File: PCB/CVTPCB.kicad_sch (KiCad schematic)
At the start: 13 parts, among them J1 Conn_01x09_Pin, J4 2x1, J7 SystemInput

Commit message: Add files via upload
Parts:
- removed C1: 0.1uf, symbol Device:C
- removed J1: Conn_01x09_Pin, symbol Connector:Conn_01x09_Pin
- removed R3, R4: R, symbol Device:R
- removed R5, R6: 22, symbol Device:R
- removed R7: 100k, symbol Device:R
- added C2, C3: 0.1uf, Capacitor_THT:C_Disc_D3.0mm_W2.0mm_P2.50mm, symbol Device:C
- added H1, H2, H3, H4: MountingHole, MountingHole:MountingHole_4.3mm_M4, symbol Mechanical:MountingHole
- added J1, J3: Infared, CVT:Infared, symbol Connector:Conn_01x04_Pin
- added J2, J5: TMP36, CVT:TMP36_Pad, symbol Connector:Conn_01x03_Pin
- added R10, R8: 300, Resistor_THT:R_Axial_DIN0204_L3.6mm_D1.6mm_P5.08mm_Horizontal, symbol Device:R
- added R11, R9: 200, Resistor_THT:R_Axial_DIN0204_L3.6mm_D1.6mm_P5.08mm_Horizontal, symbol Device:R
- added R12: 22, Resistor_THT:R_Axial_DIN0204_L3.6mm_D1.6mm_P5.08mm_Horizontal, symbol Device:R
- added R13: R, Resistor_THT:R_Axial_DIN0204_L3.6mm_D1.6mm_P5.08mm_Horizontal, symbol Device:R
- added RV1, RV2: 0-10k, Potentiometer_THT:Potentiometer_Bourns_3339H_Vertical, symbol Device:R_Potentiometer
- J4: footprint CONN_S2B-PH-K-S_JST -> Connector_PinHeader_1.00mm:PinHeader_1x02_P1.00mm_Vertical
- J7: footprint (none) -> CVT:JST4Pin
- R1: value 200 -> R; footprint (none) -> Resistor_THT:R_Axial_DIN0204_L3.6mm_D1.6mm_P5.08mm_Horizontal
- R2: value 300 -> 22; footprint (none) -> Resistor_THT:R_Axial_DIN0204_L3.6mm_D1.6mm_P5.08mm_Horizontal
- U3: footprint ESP 32:ESP 32 BAJA -> CVT:ESP 32 BAJA
- U4: footprint (none) -> CVT:1x7 Connectors
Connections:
- net +5V: now also R2.2, J1.1 (IR+), J2.2 (3.3+), J3.1 (IR+), J5.2 (3.3+), R12.2
- net CanRX: now also U3.24 (D26); no longer U3.14 (D22)
- net CanTX: now also U3.25 (D27); no longer U3.11 (D21)
- net GND: now also C2.1, C3.1, J1.3 (E-), J2.3 (GND), J3.3 (E-), J5.3 (GND), R10.2, R8.2, RV1.3, RV2.3; no longer R2.2
- net at R1.1: now also J1.2 (IR-)
- net TMP36_2: now reaches U3.27 (D12)
- net TMP36_2: now also R8.1, R9.2
- net TMP36_1: now reaches U3.28 (D13)
- net TMP36_1: now also R10.1, R11.2
- net E-1 renamed Ir1
- net Ir1: now also R13.2, RV1.1, RV1.2
- net E-2 renamed Ir2
- net Ir2: now also R1.2, RV2.1, RV2.2
- net R+1: no longer names the net of U3.22 (D33)
- net R+2: no longer names the net of U3.21 (D32)
- removed net TMP36_out: R1.2, R2.1, U3.25 (D27)
- new net: J3.2 (IR-), R13.1
- new net: J3.4 (E+), R12.1
- new net: J1.4 (E+), R2.1
- new net: C3.2, J5.1 (s), R11.1
- new net: C2.2, J2.1 (s), R9.1
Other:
- moved on the sheet: J4, J7, U3, U4

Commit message: Add files via upload
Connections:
- net CanTX: now also U3.23 (D25); no longer U3.25 (D27)
- net Ir2: now also U3.28 (D13); no longer U3.19 (D34)
- net TMP36_1: now also U3.19 (D34); no longer U3.28 (D13)
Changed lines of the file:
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@@
+	(wire
+		(pts
+			(xy 113.03 73.66) (xy 115.57 73.66)
+		)
+		(stroke
+			(width 0)
+			(type default)
+		)
+	)
 	(wire
 		(pts
@@
 	(wire
 		(pts
-			(xy 113.03 99.06) (xy 115.57 99.06)
-		)
-		(stroke
-			(width 0)
-			(type default)
-		)
-	)
-	(wire
-		(pts
 			(xy 156.21 148.59) (xy 167.64 148.59)
 		)
@@
 	(wire
 		(pts
-			(xy 113.03 73.66) (xy 115.57 73.66)
-		)
-		(stroke
-			(width 0)
-			(type default)
-		)
-	)
-	(wire
-		(pts
 			(xy 140.97 63.5) (xy 140.97 64.77)
 		)
@@
 	(wire
 		(pts
+			(xy 113.03 93.98) (xy 115.57 93.98)
+		)
+		(stroke
+			(width 0)
+			(type default)
+		)
+	)
+	(wire
+		(pts
 			(xy 148.59 135.89) (xy 151.13 135.89)
 		)
@@
 		)
 	)
-	(label "TMP36_1"
+	(label "Ir2"
 		(at 115.57 73.66 0)
+		(fields_autoplaced yes)
+		(effects
+			(font
+				(size 1.27 1.27)
+			)
+			(justify left bottom)
+		)
+	)
+	(label "CanTX"
+		(at 115.57 93.98 0)
 		(fields_autoplaced yes)
 		(effects
@@
 		)
 	)
-	(label "CanTX"
-		(at 115.57 99.06 0)
-		(fields_autoplaced yes)
-		(effects
-			(font
-				(size 1.27 1.27)
-			)
-			(justify left bottom)
-		)
-	)
 	(label "CanL"
 		(at 140.97 87.63 180)
@@
 		)
 	)
-	(label "Ir2"
-		(at 115.57 106.68 0)
-		(fields_autoplaced yes)
-		(effects
-			(font
-				(size 1.27 1.27)
-			)
-			(justify left bottom)
-		)
-	)
 	(label "CanTX"
 		(at 137.16 76.2 180)
@@
 		(fields_autoplaced yes)
 		(effects
+			(font
+				(size 1.27 1.27)
+			)
+			(justify left bottom)
+		)
+	)
+	(label "TMP36_1"
+		(at 115.57 106.68 0)
+		(fields_autoplaced yes)
+		(effects

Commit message: Add files via upload
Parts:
- removed J4: 2x1, Connector_PinHeader_1.00mm:PinHeader_1x02_P1.00mm_Vertical, symbol 2x1:S2B-PH-K-SLFSN
- removed R13: R, Resistor_THT:R_Axial_DIN0204_L3.6mm_D1.6mm_P5.08mm_Horizontal, symbol Device:R
- added J4: Conn_01x04_Pin, CVT:PowerBoard, symbol Connector:Conn_01x04_Pin
- added R3: R, Resistor_THT:R_Axial_DIN0411_L9.9mm_D3.6mm_P12.70mm_Horizontal, symbol Device:R
- R1, R10, R11, R12, R2, R8, R9: footprint Resistor_THT:R_Axial_DIN0204_L3.6mm_D1.6mm_P5.08mm_Horizontal -> Resistor_THT:R_Axial_DIN0411_L9.9mm_D3.6mm_P12.70mm_Horizontal
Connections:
- net +5V: now also J4.1 (Pin_1); no longer J1.1 (IR+)
- net GND: now also R1.2, RV1.1, RV2.1, J4.2 (Pin_2), J4.4 (Pin_4), R3.2; no longer J1.3 (E-), RV1.3, RV2.3
- net Ir1: no longer RV1.1
- net Ir2: no longer R1.2, RV2.1
- net IrOut2: now reaches J3.2 (IR-)
- net IrOut2: now also RV1.3, U3.26 (D14), R3.1
- net IrOut1: now reaches J1.2 (IR-), R1.1
- net IrOut1: now also RV2.3, U3.22 (D33)
- net +12V renamed +12v
- net +12v: now also J4.3 (Pin_3)

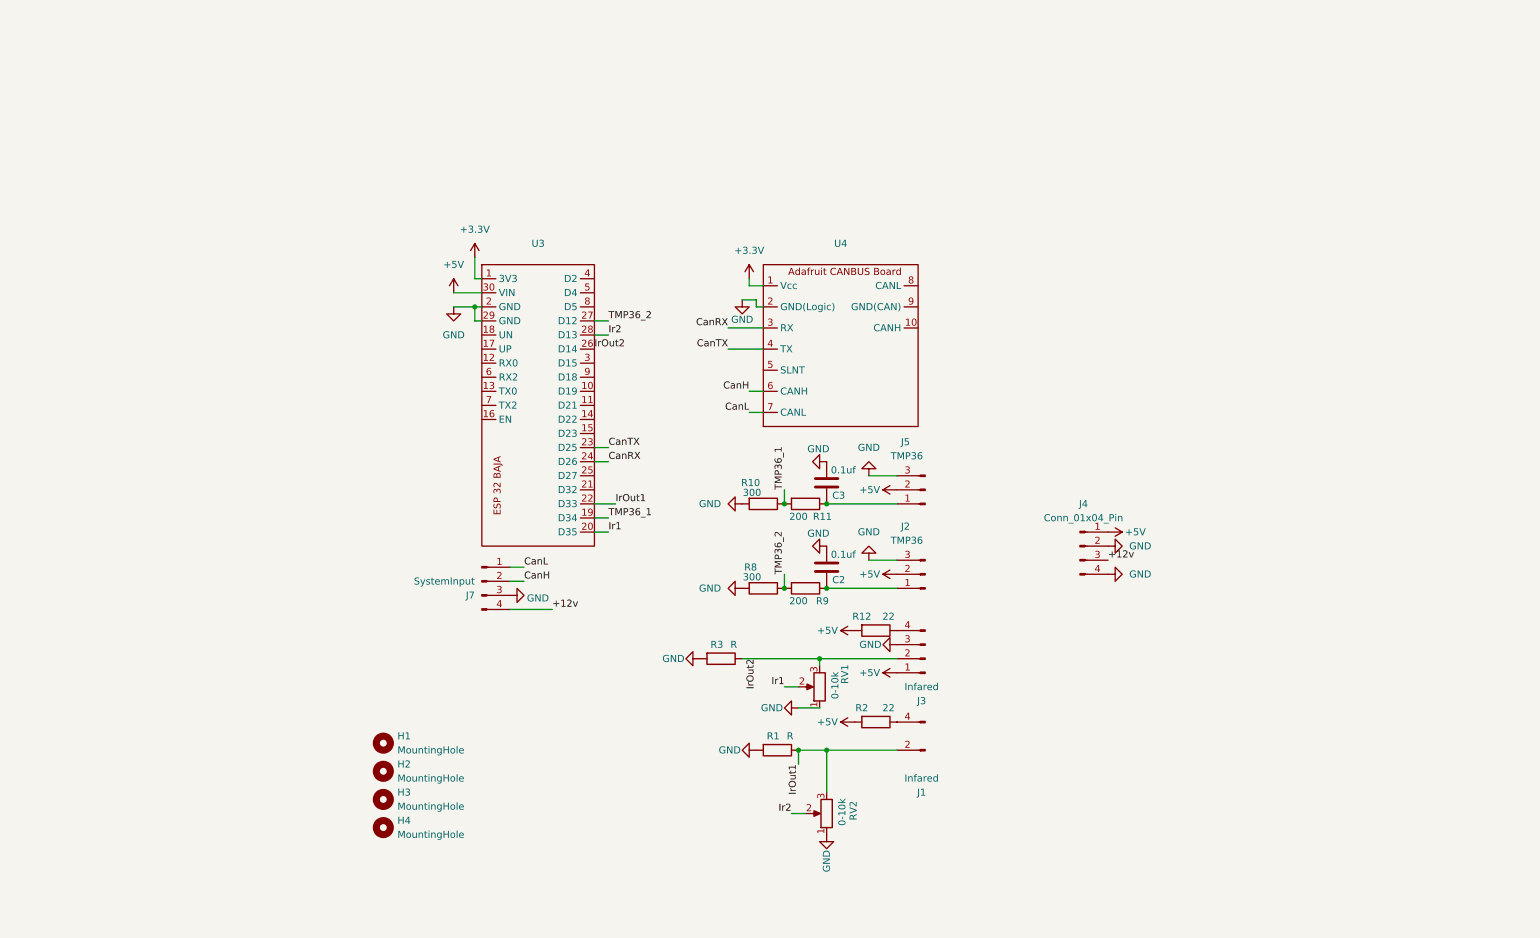
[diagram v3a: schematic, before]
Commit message: Various changes to PCB design
Changes:
Move 4 pin aviation plug connector to bottom of PCB
Move 0.1uF bypass capacitors from Vout to Vs
Remove voltage divider on TMP36 output. TMP36 output ranges from 0.1V to 2.0V, which is within our 0-3.3V reading range on ESP32
Change signal voltage divider for IR receiver from 1W footprint to 1/4W footprint
Combine +5V and GND pads for IR and TMP36
Update Silkscreen and Labels for clarity
Make Power pads SMD
Move all components to top side
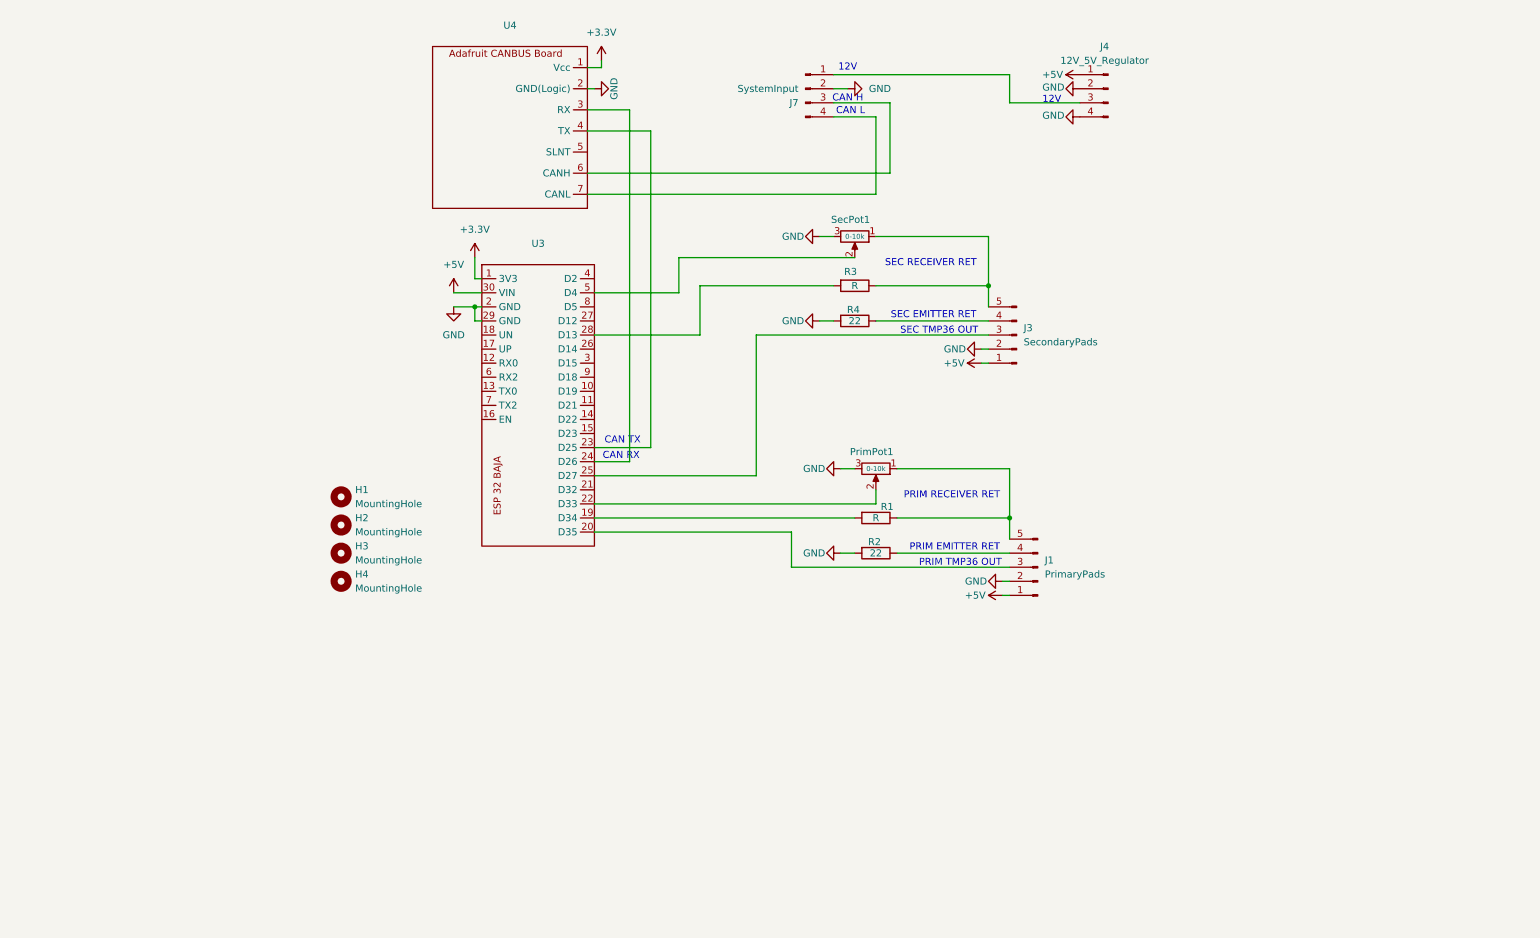
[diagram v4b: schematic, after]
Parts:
- removed C2, C3: 0.1uf, Capacitor_THT:C_Disc_D3.0mm_W2.0mm_P2.50mm, symbol Device:C
- removed J1: Infared, CVT:Infared, symbol Connector:Conn_01x04_Pin
- removed J2, J5: TMP36, CVT:TMP36_Pad, symbol Connector:Conn_01x03_Pin
- removed R10, R8: 300, Resistor_THT:R_Axial_DIN0411_L9.9mm_D3.6mm_P12.70mm_Horizontal, symbol Device:R
- removed R11, R9: 200, Resistor_THT:R_Axial_DIN0411_L9.9mm_D3.6mm_P12.70mm_Horizontal, symbol Device:R
- removed R12: 22, Resistor_THT:R_Axial_DIN0411_L9.9mm_D3.6mm_P12.70mm_Horizontal, symbol Device:R
- removed RV2: 0-10k, Potentiometer_THT:Potentiometer_Bourns_3339H_Vertical, symbol Device:R_Potentiometer
- added J1: PrimaryPads, CVT:Temp_IR_5_Pad_Combo, symbol Connector:Conn_01x05_Pin
- added PrimPot1: 0-10k, Potentiometer_THT:Potentiometer_Bourns_3339H_Vertical, symbol Device:R_Potentiometer
- added R4: 22, Resistor_THT:R_Axial_DIN0411_L9.9mm_D3.6mm_P12.70mm_Horizontal, symbol Device:R
- J3: value Infared -> SecondaryPads; footprint CVT:Infared -> CVT:Temp_IR_5_Pad_Combo; symbol Connector:Conn_01x04_Pin -> Connector:Conn_01x05_Pin
- J4: value Conn_01x04_Pin -> 12V_5V_Regulator
- R1, R3: footprint Resistor_THT:R_Axial_DIN0411_L9.9mm_D3.6mm_P12.70mm_Horizontal -> Resistor_THT:R_Axial_DIN0207_L6.3mm_D2.5mm_P10.16mm_Horizontal
- renumbered RV1 to SecPot1
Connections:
- net +5V: now also J1.1 (Pin_1); no longer R2.2
- net GND: now also J3.2 (Pin_2), J7.2 (Pin_2), R2.2, SecPot1.3, J1.2 (Pin_2), PrimPot1.3, R4.2; no longer J3.3 (E-), J7.3 (Pin_3), R1.2, R3.2, SecPot1.1
- net at J3.4 (Pin_4): now also R4.1
- net at R2.1: now also J1.4 (Pin_4)
- net at U3.25 (D27): now also J3.3 (Pin_3)
- net at U3.5 (D4): now also SecPot1.2
- net +12v: no longer names the net of J4.3 (Pin_3)
- net +12v: now also J7.1 (Pin_1); no longer J7.4 (Pin_4)
- net CanH: no longer names the net of U4.6 (CANH)
- net CanH: now also J7.3 (Pin_3); no longer J7.2 (Pin_2)
- net CanL: no longer names the net of U4.7 (CANL)
- net CanL: now also J7.4 (Pin_4); no longer J7.1 (Pin_1)
- net CanRX: no longer names the net of U3.24 (D26), U4.3 (RX)
- net CanTX: no longer names the net of U3.23 (D25), U4.4 (TX)
- net Ir1: no longer names the net of U3.20 (D35)
- net Ir1: now also J1.3 (Pin_3); no longer SecPot1.2
- net Ir2: no longer names the net of U3.28 (D13)
- net Ir2: now also R3.2
- net IrOut1: no longer names the net of R1.1
- net IrOut1: now also J1.5 (Pin_5), PrimPot1.1; no longer U3.22 (D33)
- removed net IrOut2: J3.2 (IR-), R3.1, SecPot1.3, U3.26 (D14)
- net TMP36_1: no longer names the net of U3.19 (D34)
- net TMP36_1: now also R1.2
- net TMP36_2: no longer names the net of U3.27 (D12)
- new net: J3.5 (Pin_5), R3.1, SecPot1.1
- new net: PrimPot1.2, U3.22 (D33)
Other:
- note added: "12V"
- note added: "CAN H"
- note added: "CAN L"
- note added: "CAN RX"
- note added: "CAN TX"
- note added: "PRIM EMITTER RET"
- note added: "PRIM RECEIVER RET"
- note added: "PRIM TMP36 OUT"
- note added: "SEC EMITTER RET"
- note added: "SEC RECEIVER RET"
- note added: "SEC TMP36 OUT"
- moved on the sheet: H1, H2, H3, H4, J4, J7, SecPot1

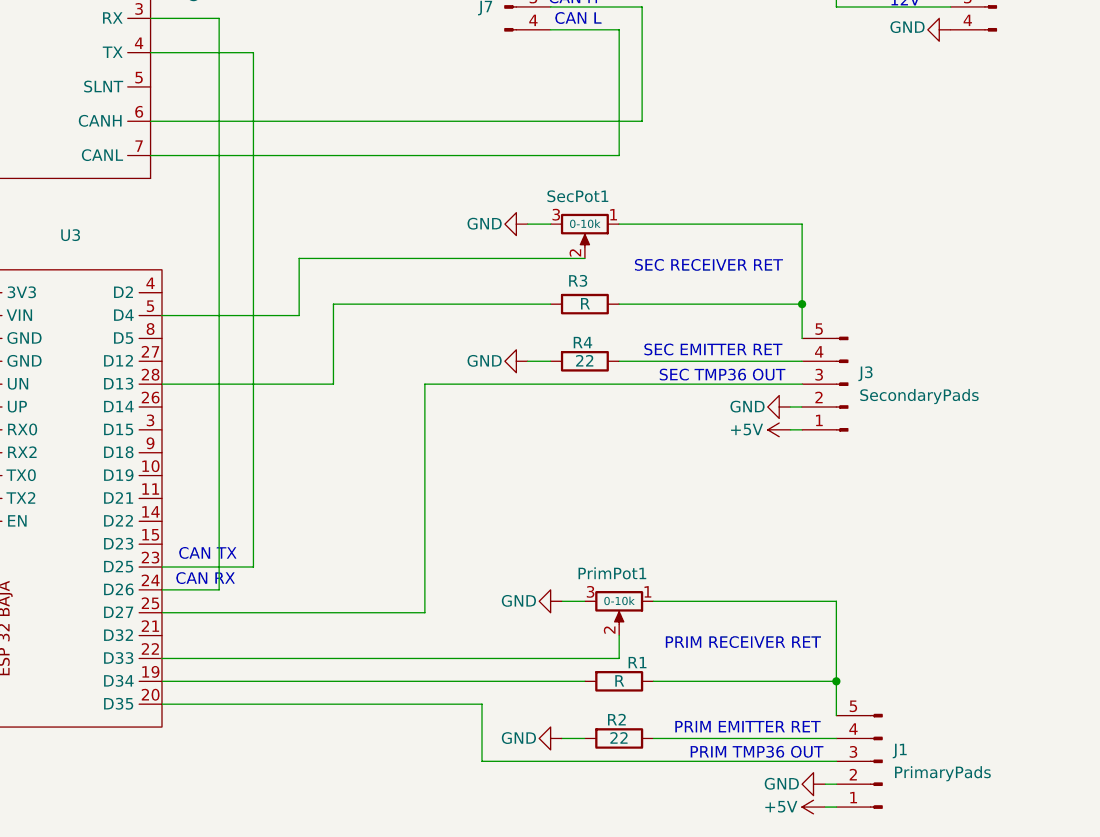
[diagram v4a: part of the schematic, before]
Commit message: Partial fix for incorrect voltage divider
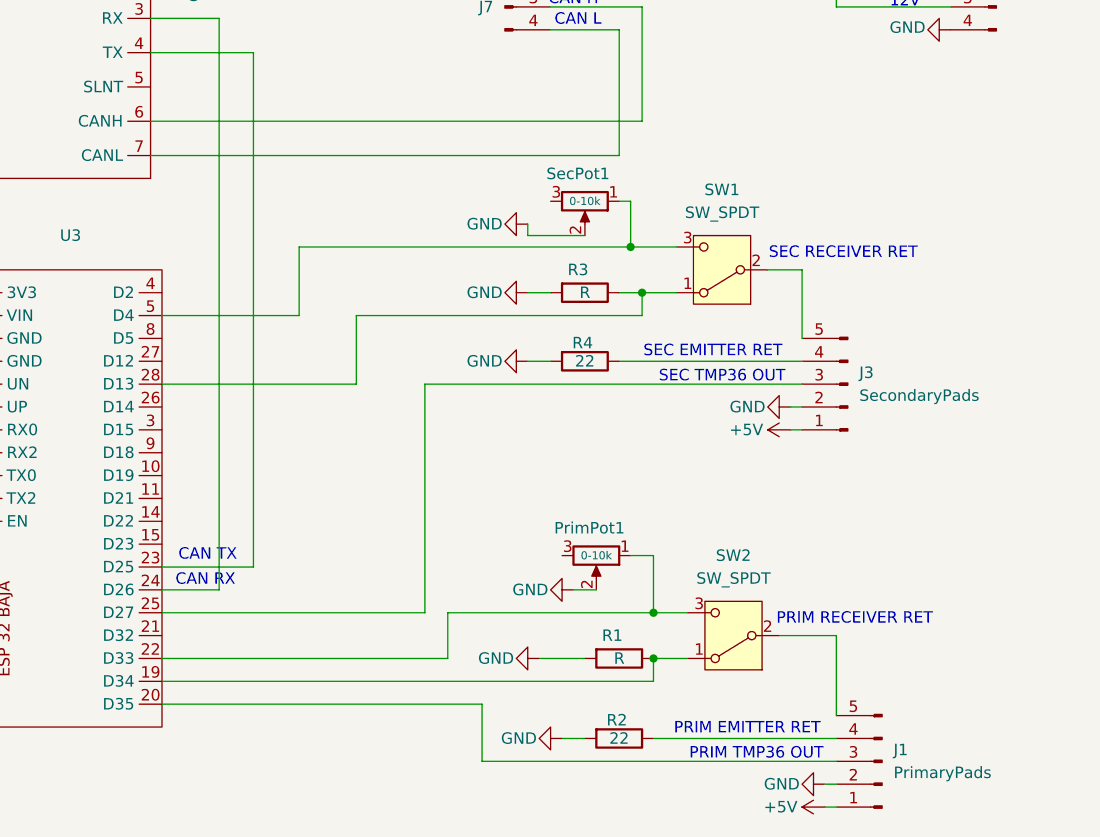
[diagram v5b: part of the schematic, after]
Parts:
- added SW1, SW2: SW_SPDT, Button_Switch_THT:SW_Slide-03_Wuerth-WS-SLTV_10x2.5x6.4_P2.54mm, symbol Switch:SW_SPDT
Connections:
- net GND: now also PrimPot1.2, R1.2, R3.2, SecPot1.2; no longer PrimPot1.3, SecPot1.3
- net at U3.19 (D34): now also R1.1, SW2.1 (A); no longer R1.2
- net at U3.28 (D13): now also R3.1, SW1.1 (A); no longer R3.2
- net at U3.22 (D33): now also PrimPot1.1, SW2.3 (C); no longer PrimPot1.2
- net at U3.5 (D4): now also SecPot1.1, SW1.3 (C); no longer SecPot1.2
- new net: J3.5 (Pin_5), SW1.2 (B)
- new net: J1.5 (Pin_5), SW2.2 (B)
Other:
- moved on the sheet: R3, SecPot1

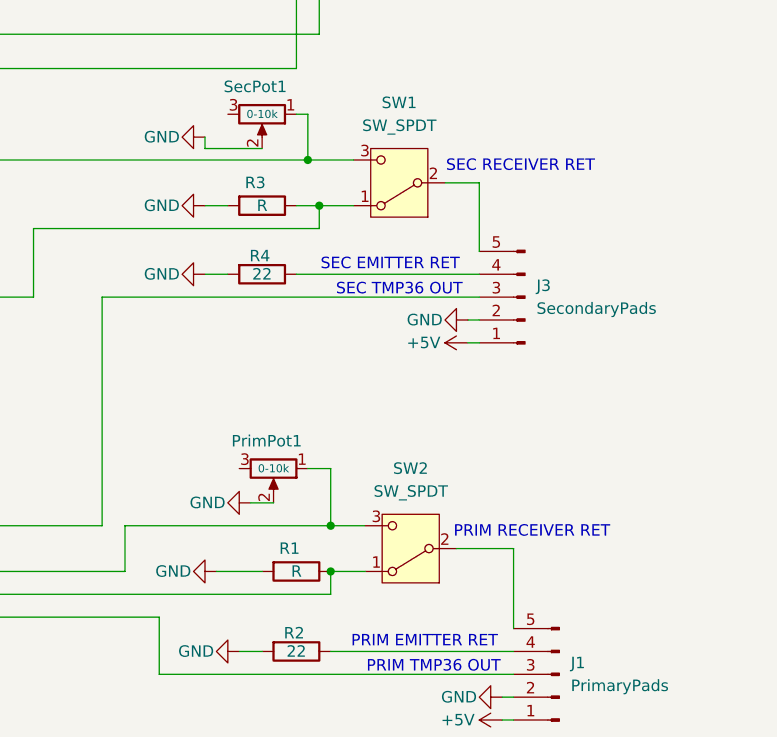
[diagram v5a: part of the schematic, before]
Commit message: Complete pot/resistor issue fix
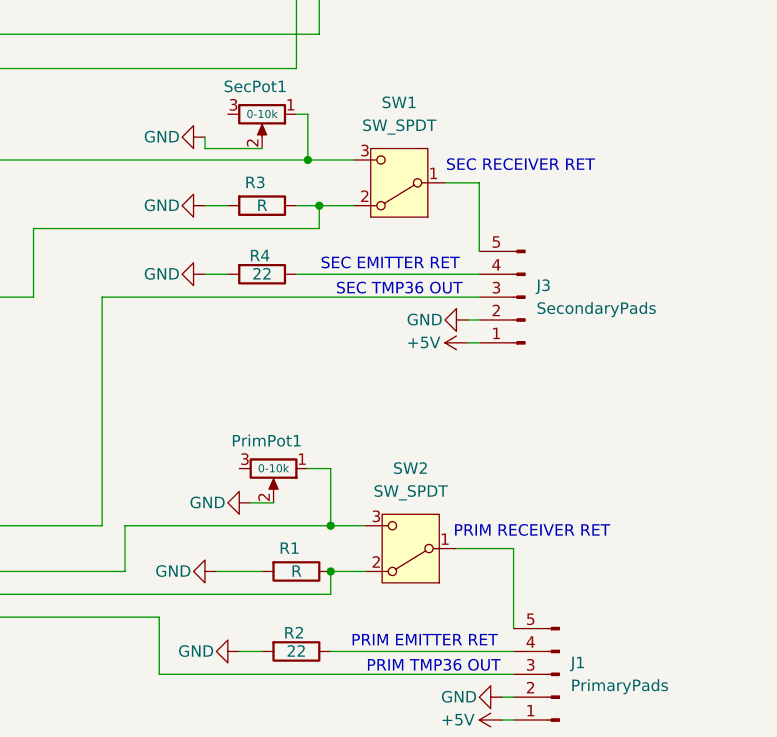
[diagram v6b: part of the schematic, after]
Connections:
- net at J3.5 (Pin_5): now also SW1.1 (B); no longer SW1.2 (B)
- net at R3.1, U3.28 (D13): now also SW1.2 (A); no longer SW1.1 (A)
- net at J1.5 (Pin_5): now also SW2.1 (B); no longer SW2.2 (B)
- net at R1.1, U3.19 (D34): now also SW2.2 (A); no longer SW2.1 (A)
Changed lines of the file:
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@@
 	)
 	(symbol
+		(lib_name "SW_SPDT_1")
 		(lib_id "Switch:SW_SPDT")
 		(at 176.53 101.6 180)
